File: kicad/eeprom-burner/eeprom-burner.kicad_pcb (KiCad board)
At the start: 2 copper layers, 53.3 x 66 mm, 9 parts

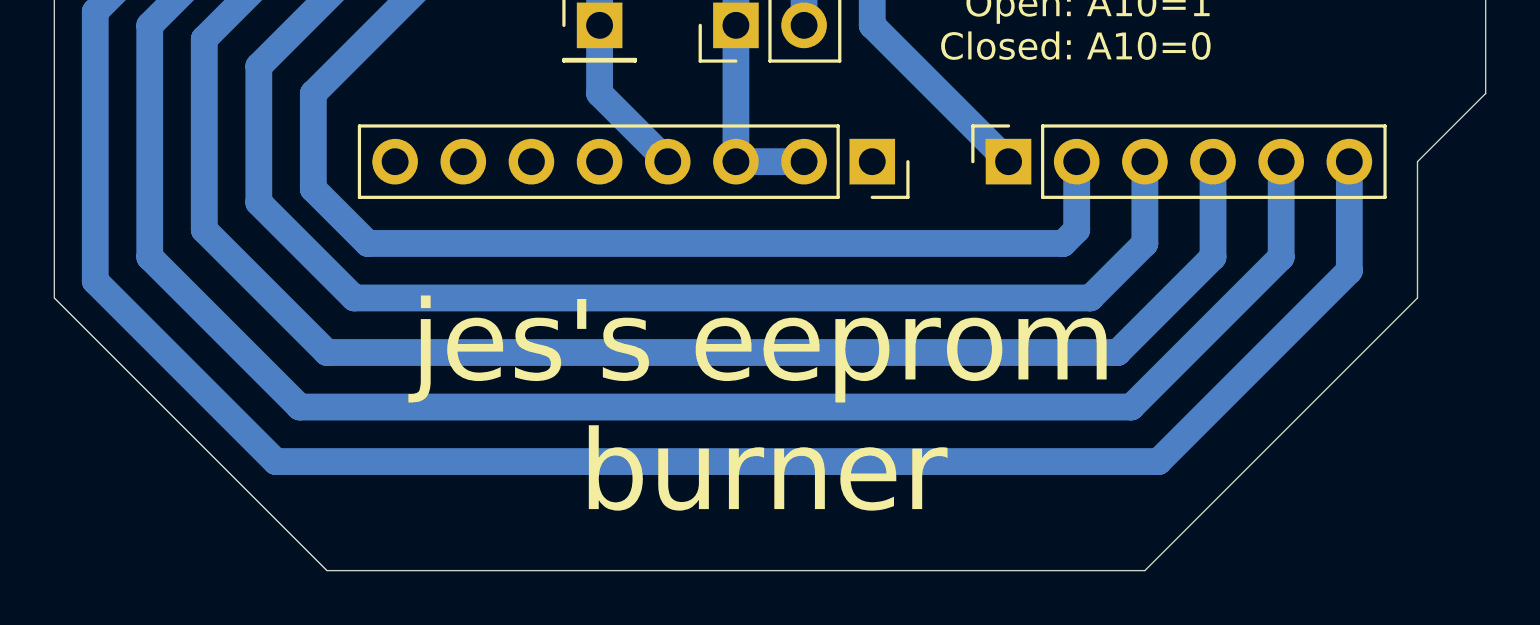
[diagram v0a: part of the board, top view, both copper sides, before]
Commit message: Make Drill.gcode, and some other G-Code changes
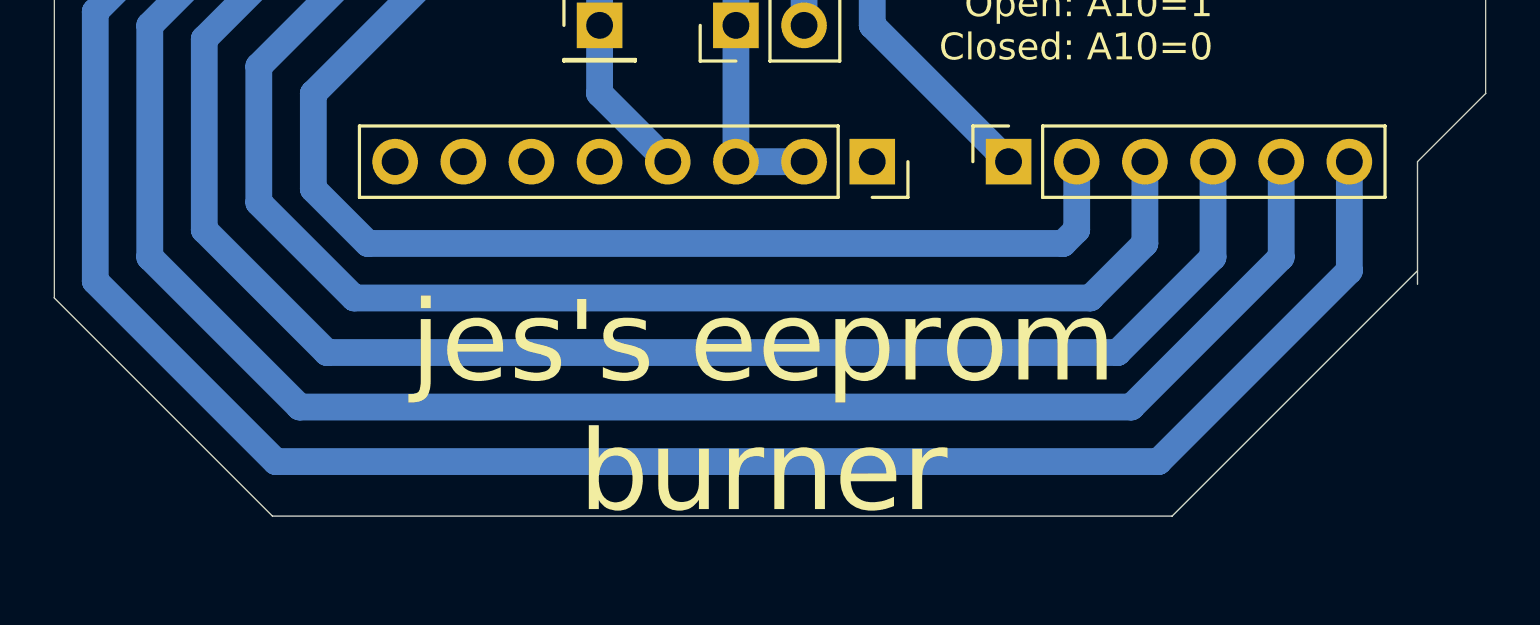
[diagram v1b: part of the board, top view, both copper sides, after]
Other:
- board size 53.3 x 66 mm -> 53.3 x 64 mm
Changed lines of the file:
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@@
     (effects (font (size 1 1) (thickness 0.15)) (justify right))
   )
-  (gr_line (start 116.84 144.78) (end 127 134.62) (layer Edge.Cuts) (width 0.05))
-  (gr_line (start 86.36 144.78) (end 116.84 144.78) (layer Edge.Cuts) (width 0.05))
-  (gr_line (start 76.2 134.62) (end 86.36 144.78) (layer Edge.Cuts) (width 0.05))
+  (gr_line (start 117.856 142.748) (end 127 133.604) (layer Edge.Cuts) (width 0.05))
+  (gr_line (start 84.328 142.748) (end 117.856 142.748) (layer Edge.Cuts) (width 0.05))
+  (gr_line (start 76.2 134.62) (end 84.328 142.748) (layer Edge.Cuts) (width 0.05))
   (gr_line (start 76.2 78.74) (end 76.2 134.62) (layer Edge.Cuts) (width 0.05))
   (gr_line (start 129.54 94.234) (end 127 91.694) (layer Edge.Cuts) (width 0.05))
   (gr_line (start 125.476 78.74) (end 127 80.264) (layer Edge.Cuts) (width 0.05))
   (gr_line (start 127 80.264) (end 127 91.694) (layer Edge.Cuts) (width 0.05))
-  (gr_line (start 127 129.54) (end 127 134.62) (layer Edge.Cuts) (width 0.05))
+  (gr_line (start 127 129.54) (end 127 134.112) (layer Edge.Cuts) (width 0.05))
   (gr_line (start 129.54 127) (end 127 129.54) (layer Edge.Cuts) (width 0.05))
   (gr_line (start 129.54 94.234) (end 129.54 127) (layer Edge.Cuts) (width 0.05))
